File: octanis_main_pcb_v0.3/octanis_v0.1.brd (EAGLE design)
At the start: 95 x 48 mm, 89 parts, among them IC1 REG1117, IC2 LM555D, Q1 32.768kHz, T1 BC547, T2 BC547, U1 BQ24210, U2 BQ27510_DRZ_12, U3 DRV8836DSSR, U4 DRV8836DSSR, U5 DRV8836DSSR, U6 MSP430F5529IPNR, U7 DRV8836DSSR, U9 BMP180

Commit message: startet new mainboard PCB
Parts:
- removed BATTERY: - BAT +, pinhead:1X02
- removed C1, C2: 1uF, rcl:C1206
- removed C26: 12p, rcl:C0603
- removed C29: 100n, rcl:C0603
- removed C7, C8: 1uF, rcl:C0603
- removed CG1, CG3, CG6, CG7, CG8: 0.1uF, rcl:C0603
- removed CG2: 33nF, rcl:C0603
- removed CG4: 0.47uF, rcl:C0603
- removed DIGITAL1: DIGITAL1, pinhead:1X06
- removed HEATPAD: HEATPAD, con-molex:22-23-2021
- removed HUMIDITY: HS1101, rcl:C025-024X044
- removed I2C: SCL SDA, pinhead:1X02
- removed IC1: REG1117, burr-brown:SOT223
- removed IC2: LM555D, linear:SO08
- removed LED2: (no value), led:CHIP-LED0603
- removed Q1: 32.768kHz, crystal:FC-12M
- removed R28: 0R, rcl:R0603
- removed RG1: 1.8M, rcl:R0603
- removed RG2: 18.2k, rcl:R0603
- removed RG3, RH3: 1k, rcl:R0603
- removed RG5, RG6: 100, rcl:R0603
- removed RH1: 909k, rcl:R0603
- removed RH2: 576k, rcl:R0603
- removed RH4: 49.9k, rcl:R0603
- removed RSBAT: 0.01, resistor:R1206
- removed RT1: 21.5k, resistor:R1206
- removed RVDM: float, resistor:R1206
- removed SOLAR: - SOLAR +, pinhead:1X02
- removed T1, T2: BC547, transistor:TO92
- removed TEMP1, TEMP2: 103AT, varistor:RS-2,5
- removed U2: BQ27510_DRZ_12, bq27510_drz_12:DRZ12_1P95X2P45
- removed U6: MSP430F5529IPNR, TI_MSP430_v16_intern:PN80
- added C22, C9: 12p, rcl:C0402
- added C23: 100n, rcl:C0402
- added C24: 100n, rcl:C0603
- added D5: 1N581D1206, lpatiny:LED-1206
- added GREEN: 3V-ok, adafruit:CHIPLED_0603
- added JP3: (no value), pinhead:1X06
- added JP4: (no value), pinhead:2X07
- added LED0: LED0, adafruit:CHIPLED_0603
- added Q2: 32.768kHz, microcrystal:MS3V-T1R
- added R17, R8, R9: 1k, rcl:R0603
- added R18, RPUC1, RPUD1: 10k, rcl:R0603
- added R7: 0R, rcl:R0402
- added U$2: F54XX[A]---PZ100, TI_MSP430_v16:PZ100
- added U$3: SST25VF064C, BertaLib:SOIC_8-LEAD
- added U$4: HX1, Octanis1:HX1
- ANALOG: device pinhead:1X06 -> pinhead:1X08
- C25: value 12p -> 100n
- DIGITAL2: device pinhead:1X08 -> pinhead:1X11
- JP1: value rst SBW tst -> RST TST
- JP2: value SERIAL -> (none); device pinhead:1X04 -> pinhead:1X02
- LED1: value (none) -> LED1; device led:CHIP-LED0603 -> adafruit:CHIPLED_0603
- R1: value 1k -> 10k
- R16: value 1M -> 10k
- R2: value 1k -> 1M
- R4: value 500 -> 1k; device resistor:R1206 -> rcl:R0603
- U1: value BQ24210 -> SHT21; device bq24210_dqc_10:DQC10_P84X2P4 -> SENSIRION-SHT21:DFN300X300X110-7N
- moved LED1 178.5 mm to (1.27, -152.4), turned to 0 degrees
- moved R4 149.9 mm to (1.27, -134.6)
- moved R2 148.9 mm to (1.27, -123.2), flipped to the top
- moved U1 129.2 mm to (6.35, -108.0), turned to 0 degrees
- moved R1 124.1 mm to (14.0, -95.2), flipped to the top
- moved R16 115.3 mm to (14.0, -80.0), turned to 0 degrees
- moved JP2 109.1 mm to (1.98, -40.6), turned to 0 degrees
- moved C25 96.5 mm to (1.27, -73.7)
- moved DIGITAL2 28.4 mm to (57.1, 39.4)
- moved ANALOG 13.1 mm to (33.0, 39.4)
- moved JP1 10.3 mm to (43.2, 35.6)
- moved RPUD 5.68 mm to (61.0, 23.5)
- renumbered LED3 to RED
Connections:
- removed net 65: U6.65
- removed net 66: U6.66
- removed net 67: U6.67
- removed net AVCC: C29.1, R28.1, U6.11
- removed net BAT-: BATTERY.2, RG6.1, RSBAT.1
- removed net CHG_EN: U1.7, U6.5
- removed net EN_BAT_HEAT: T2.2
- removed net EN_SOLAR_HEAT: T1.2
- removed net HUMOUT: RH3.1
- removed net M1234SLEEP: U3.11, U3.12, U4.11, U4.12, U6.21
- removed net M5678SLEEP: U5.11, U5.12, U6.35, U7.11, U7.12
- removed net N$29: HUMIDITY.1, IC2.2, IC2.6, RH2.2
- removed net N$3: LED2.A, R2.1
- removed net N$33: RG2.1, RG3.2, TEMP2.1
- removed net N$34: CG1.1, RG3.1, U2.9
- removed net N$35: CG4.1, RG1.2, U2.2, U2.5
- removed net N$36: CG6.1, CG7.1, RG5.2, U2.8
- removed net N$37: HEATPAD.1, T1.1, T2.1
- removed net N$38: CG6.2, CG8.2, RG6.2, U2.7
- removed net N$8: RT1.2, U1.4
- removed net P2.7: DIGITAL1.6, U6.36
- removed net P3.0: DIGITAL1.5, U6.37
- removed net P3.1: DIGITAL1.4, U6.38
- removed net P3.2: DIGITAL1.3, U6.39
- removed net P3.3: DIGITAL1.2, U6.40
- removed net P3.4: DIGITAL1.1, U6.41
- removed net P3.5: U6.42
- removed net P3.6: U6.43
- removed net P3.7: U6.44
- removed net P5.0: ANALOG.2, U6.9
- removed net P5.1: ANALOG.1, U6.10
- removed net P5.4/XIN: C26.2, Q1.2, U6.12
- removed net P5.5/XOUT: C25.2, Q1.1, U6.13
- removed net P6.0: U6.77
- removed net P6.1: U6.78
- removed net P6.2: U6.79
- removed net P6.3: U6.80
- removed net P6.4: ANALOG.6, U6.1
- removed net P6.5: ANALOG.5, U6.2
- removed net P6.6: ANALOG.4, U6.3
- removed net P6.7: ANALOG.3, U6.4
- removed net RST/SBWTDIO: JP1.1, U6.76
- removed net SPI_CLK: JP2.1, U6.45
- removed net TARGET_DP: U6.62
- removed net TARGET_PUR: R16.2, U6.63
- removed net TEST/SBWTCK: JP1.2, U6.71
- removed net VCC: C1.1, SOLAR.2, T1.3, U1.1
- new net 3.3V: C3.1, GREEN.A, JP4.7, JP4.8, L1.P$1, R1.2, R16.2, R2.2, U$1.10, U$3.RST/HOLD, U$3.VDD, U$3.WP
- new net AVCC1: C23.1, R7.1, U$2.11
- new net CS: R17.2
- new net FMOSI: D5.A, R1.1, U$3.SI
- new net HX1EN: U$4.EN
- new net HX1TX: U$4.TXD
- new net LED0: LED0.A, U$2.9
- new net LED1: LED1.A, U$2.10
- new net M12SLEEP: U$2.18, U3.11, U3.12
- new net M34SLEEP: U$2.23, U4.11, U4.12
- new net M56SLEEP: U$2.40
- new net M78SLEEP: U$2.45, U5.11, U5.12, U7.11, U7.12
- new net N$28: ANALOG.7, U$2.98
- new net N$73: ANALOG.5, U$2.100
- new net N$74: ANALOG.4, U$2.1
- new net N$75: ANALOG.3, U$2.2
- new net N$76: ANALOG.2, U$2.3
- new net N$77: ANALOG.1, U$2.4
- new net N$78: DIGITAL2.10, U$2.77
- new net N$79: DIGITAL2.11, U$2.76
- new net P5.4/XIN1: C22.2, Q2.P2, U$2.13
- new net P5.5/XOUT1: C9.2, Q2.P1, U$2.14
- new net RFGND: U$4.RFGND
- new net RFGND2: U$4.RFGND2
- new net RST: JP1.1, U$2.96
- new net SCL2: JP4.2, RPUC.1, U$2.70
- new net SDA2: JP4.1, RPUD.1, U$2.69
- new net SPI_MISO: U$3.SO
- new net SPI_SCK: JP3.3, R18.1, U$2.68
- new net SPI_SIMO: D5.C, JP3.5, U$2.72
- new net SPI_SOMI: JP3.6, U$2.73
- new net TST: JP1.2, U$2.91
- net +3V3: now also C24.1, C25.1, R7.2, RPUC1.2, RPUD1.2, U$2.16, U$2.38, U$2.64, U$2.87; no longer C8.1, IC1.2, IC2.4, IC2.8, R28.2, RH4.1, U6.18, U6.50
- net +5V: now also JP4.13, JP4.14
- net 5VEN: now also R2.1; no longer U6.6
- net BAT+: now also U$4.VCC; no longer BATTERY.1, C2.1, C3.1, C7.1, CG3.1, IC1.3, L1.P$1, R1.2, R2.2, T2.3, U$1.10, U1.10, U2.3, U2.4
- net GND: now also C22.1, C23.2, C24.2, C25.2, C9.1, JP4.11, JP4.12, JP4.3, JP4.4, JP4.5, JP4.6, Q2.P3, R8.1, R9.1, U$2.12, U$2.15, U$2.37, U$2.63, U$2.88, U$3.VSS, U1.2; no longer C1.2, C2.2, C25.1, C26.1, C29.2, C7.2, C8.2, CG1.2, CG2.2, CG3.2, CG4.2, CG7.2, CG8.1, HEATPAD.2, HUMIDITY.2, IC1.1, IC2.1, R16.1, RG5.1, RH1.1, RSBAT.2, RVDM.1, SOLAR.1, TEMP1.1, TEMP2.2, U1.11, U1.3, U2.13, U2.6, U2.V, U2.V_2, U2.V_3, U2.V_4, U2.V_5, U2.V_6, U6.14, U6.19, U6.49, U6.61, U6.68
- net M1IN1: now also U$2.19; no longer U6.15
- net M1IN2: now also U$2.20; no longer U6.22
- net M2IN1: now also U$2.21; no longer U6.16
- net M2IN2: now also U$2.22; no longer U6.23
- net M3IN1: now also U$2.24; no longer U6.17
- net M3IN2: now also U$2.26; no longer U6.24
- net M4IN1: now also U$2.27; no longer U6.25
- net M4IN2: now also U$2.28; no longer U6.26
- net M5IN1: now also U$2.41; no longer U6.27
- net M5IN2: now also U$2.42; no longer U6.28
- net M6IN1: now also U$2.43; no longer U6.29
- net M6IN2: now also U$2.44; no longer U6.30
- net M7IN1: now also U$2.46; no longer U6.31
- net M7IN2: now also U$2.47; no longer U6.32
- net M8IN1: now also U$2.48; no longer U6.33
- net M8IN2: now also U$2.49; no longer U6.34
- net N$1: now also R18.2, U$3.SCK; no longer CG2.1, RG1.1, RG2.2, U2.1
- net N$10: now also R16.1, R17.1, U$3.CE; no longer R4.2, U1.2
- net N$14: now also U$2.86; no longer U6.60
- net N$15: now also U$2.85; no longer U6.59
- net N$2: now also U1.5; no longer LED1.A, R1.1
- net N$20: now also U$2.84; no longer U6.58
- net N$21: now also U$2.83; no longer U6.57
- net N$22: now also U$2.82; no longer U6.56
- net N$23: now also U$2.81; no longer U6.55
- net N$24: now also U$2.80; no longer U6.54
- net N$26: now also U$2.79; no longer U6.53
- net N$27: now also ANALOG.8, U$2.97; no longer IC2.5, RH1.2
- net N$30: now also ANALOG.6, U$2.99; no longer IC2.7, RH2.1, RH4.2
- net N$31: now also DIGITAL2.9, U$2.78; no longer IC2.3, RH3.2
- net N$4: now also GREEN.C, R4.2; no longer LED1.C, U1.8
- net N$5: now also LED0.C, R8.2; no longer LED2.C, U1.6
- net N$6: now also LED1.C, R9.2; no longer RVDM.2, U1.9
- net N$7: now also JP4.10, JP4.9; no longer RT1.1, TEMP1.2, U1.5
- net RX: now also JP2.1, U$2.54; no longer JP2.3, U6.52
- net SCL: now also JP3.1, RPUC1.1, U$2.35, U1.6; no longer I2C.1, RPUC.1, U2.11, U6.47
- net SDA: now also JP3.2, RPUD1.1, U$2.34, U1.1; no longer I2C.2, RPUD.1, U2.10, U6.46
- net SPI_SLAVE_EN: now also JP3.4, U$2.71; no longer JP2.4, U6.48
- net TX: now also U$2.53; no longer U6.51
- net VCORE: now also U$2.62; no longer U6.20
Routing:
- net BAT+: track 103.6 -> 0.00 mm, vias 3 -> 0
- net +5V: track 10.3 -> 59.3 mm, vias 0 -> 4
- net VCC: track 36.4 -> 0.00 mm
- net +3V3: track 7.05 -> 42.9 mm, vias 0 -> 2
- net M2IN2: track 0.00 -> 27.9 mm, vias 0 -> 2
- net M1IN2: track 0.00 -> 26.1 mm
- net M2IN1: track 0.00 -> 22.7 mm, vias 0 -> 2
- net CHG_EN: track 20.4 -> 0.00 mm, vias 4 -> 0
- net GND: track 39.7 -> 59.8 mm, vias 10 -> 19
- net N$1: track 17.0 -> 0.00 mm, vias 2 -> 0
- net N$7: track 16.7 -> 0.00 mm, vias 1 -> 0
- net N$38: track 16.6 -> 0.00 mm, vias 2 -> 0
- net N$49: track 0.00 -> 15.5 mm
- net N$58: track 0.00 -> 15.5 mm
- net M3IN2: track 0.00 -> 14.3 mm
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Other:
- board size 95 x 48 mm -> 94.9 x 47.8 mm

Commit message: added aria bob
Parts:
- removed RPUC1, RPUD1: 10k, rcl:R0603
- added RPUC2, RPUD2: 10k, rcl:R0603
- moved LED1 172.6 mm to (21.6, 19.1)
- moved R8 172.6 mm to (21.6, 25.4)
- moved LED0 172.6 mm to (21.6, 30.5)
- moved R4 172.6 mm to (21.6, 36.8)
- moved R9 172.6 mm to (21.6, 14.0)
- moved GREEN 158.9 mm to (8.89, 29.2)
- moved R2 149.2 mm to (15.2, 25.4)
- moved R1 145.9 mm to (90.2, 29.2)
- moved R16 145.9 mm to (90.2, 44.5)
- moved R17 145.9 mm to (77.5, 29.2)
- moved U1 145.9 mm to (82.5, 16.5)
- moved R18 145.9 mm to (83.8, 29.2)
- moved U$3 145.9 mm to (81.3, 36.8)
- moved D5 145.9 mm to (78.7, 24.1)
- moved JP2 101.5 mm to (88.3, 12.7)
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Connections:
- net +3V3: now also RPUC2.2, RPUD2.2; no longer RPUC1.2, RPUD1.2
- net SCL: now also RPUC.1; no longer RPUC1.1
- net SCL2: now also RPUC2.1; no longer RPUC.1
- net SDA: now also RPUD.1; no longer RPUD1.1
- net SDA2: now also RPUD2.1; no longer RPUD.1

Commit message: starting layout v0.3
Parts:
- removed R5: 68k, rcl:R0603
- removed RPUC2, RPUD2: 10k, rcl:R0603
- added C1: 100n, rcl:C0603
- added C2: 100nF, rcl:C0603
- added C26, C27, C28, C8: 470n, rcl:C0603
- added C7: 22uF, rcl:C0603
- added SJ1: (no value), jumper:SJ_2
- C15: value 0.1uF -> 100nF
- R3: value 270k -> 1M
- U$1: value TPS61230 -> TPS61232; device texas:DRC-S-PVSON-N11 -> texasinstruments:S-PVSON-N10
- moved C21 90.6 mm to (5.71, 35.6), turned to 0 degrees
- moved C17 85.5 mm to (11.4, 34.3), turned to 180 degrees
- moved MPU-6050 84.2 mm to (5.97, 30.6), turned to 90 degrees
- moved C16 82.2 mm to (11.4, 31.8), turned to 180 degrees
- moved C20 78.9 mm to (11.4, 29.2), turned to 0 degrees
- moved U9 75.5 mm to (3.58, 22.6), turned to 270 degrees
- moved C11 71.9 mm to (11.4, 23.6), turned to 0 degrees
- moved U1 71.3 mm to (15.2, 40.0)
- moved C10 69.6 mm to (8.26, 36.2)
- moved C13 69.6 mm to (8.26, 40.0)
- moved C15 69.6 mm to (7.62, 43.8)
- moved COMPASS 69.6 mm to (4.85, 40.3)
- moved R7 69.6 mm to (2.16, 44.7)
- moved C12 69.0 mm to (10.8, 21.0), turned to 180 degrees
- moved RPUD 54.3 mm to (1.91, 18.4), turned to 180 degrees
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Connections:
- net SPI_SLAVE_EN renamed SPI_EXTSLAVE_TE
- removed net BAT+: U$4.VCC
- removed net CS: R17.2
- removed net HX1TX: U$4.TXD
- removed net M12SLEEP: U$2.18, U3.11, U3.12
- removed net M34SLEEP: U$2.23, U4.11, U4.12
- removed net M56SLEEP: U$2.40
- removed net M78SLEEP: U$2.45, U5.11, U5.12, U7.11, U7.12
- removed net N$43: R3.1, R5.2, U$1.7
- removed net N$7: JP4.10, JP4.9
- removed net PG: U$1.5
- removed net RFGND2: U$4.RFGND2
- new net M1234SLEEP: U$2.24, U3.11, U3.12, U4.11, U4.12
- new net M5678SLEEP: U$2.50, U5.11, U5.12, U7.11, U7.12
- new net SPI_FLASH_CS: R17.2, U$2.75
- new net V_MOTOR: C26.2, C27.2, C28.2, C8.2, SJ1.2, U3.1, U4.1, U5.1, U7.1
- net +3V3: now also C1.1, C3.1, GREEN.A, JP4.10, JP4.7, JP4.8, JP4.9, L1.P$1, R1.2, R16.2, R2.2, SJ1.1, U$1.10, U$3.RST/HOLD, U$3.VDD, U1.5; no longer RPUC2.2, RPUD2.2
- net +5V: now also C2.1, C7.1, SJ1.3, U$1.7, U$4.VCC; no longer U3.1, U4.1, U5.1, U7.1
- net 3.3V: no longer C3.1, GREEN.A, JP4.7, JP4.8, L1.P$1, R1.2, R16.2, R2.2, U$1.10, U$3.RST/HOLD, U$3.VDD
- net 5VEN: now also U$2.17
- net GND: now also C1.2, C2.2, C26.1, C27.1, C28.1, C7.2, C8.1, U$1.EXPAD, U$4.0V; no longer R5.1, U$1.GND, U$1.GND@1, U$1.GND@2, U$1.GND@3, U$1.GND@4, U$1.GND@5
- net M1IN1: now also U$2.25; no longer U$2.19
- net M1IN2: now also U$2.26; no longer U$2.20
- net M2IN1: now also U$2.27; no longer U$2.21
- net M2IN2: now also U$2.28; no longer U$2.22
- net M3IN1: now also U$2.42; no longer U$2.24
- net M3IN2: now also U$2.43; no longer U$2.26
- net M4IN1: now also U$2.44; no longer U$2.27
- net M4IN2: now also U$2.45; no longer U$2.28
- net M5IN1: now also U$2.46; no longer U$2.41
- net M5IN2: now also U$2.47; no longer U$2.42
- net M6IN1: now also U$2.48; no longer U$2.43
- net M6IN2: now also U$2.49; no longer U$2.44
- net M7IN1: now also U$2.56; no longer U$2.46
- net M7IN2: now also U$2.57; no longer U$2.47
- net M8IN1: now also U$2.58; no longer U$2.48
- net M8IN2: now also U$2.59; no longer U$2.49
- net N$2: now also R3.1, U$1.5; no longer U1.5
- net RFGND: now also U$4.RFGND2
- net SCL: now also JP4.2
- net SCL2: no longer JP4.2, RPUC2.1
- net SDA: now also JP4.1
- net SDA2: no longer JP4.1, RPUD2.1
- net TX: now also U$4.TXD
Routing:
- net +5V: track 59.3 -> 117.7 mm, vias 4 -> 3
- net V_MOTOR: track 0.00 -> 41.6 mm, vias 0 -> 4
- net GND: track 59.8 -> 22.6 mm, vias 19 -> 13
- net 5VEN: track 0.00 -> 23.4 mm, vias 0 -> 2
- net M1234SLEEP: track 0.00 -> 22.0 mm, vias 0 -> 2
- net M5678SLEEP: track 0.00 -> 18.8 mm, vias 0 -> 2
- net N$43: track 16.9 -> 0.00 mm
- net M1IN1: track 0.00 -> 15.6 mm
- net M2IN2: track 27.9 -> 15.1 mm, vias 2 -> 0
- net SCL: track 12.4 -> 0.00 mm
- net M1IN2: track 26.1 -> 15.1 mm
- net SDA: track 10.7 -> 0.00 mm
- net M8IN1: track 10.4 -> 2.34 mm
- net M2IN1: track 22.7 -> 15.1 mm, vias 2 -> 0
- net +3V3: track 42.9 -> 35.8 mm, vias 2 -> 1
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- added copper zone on layer 1, net +3V3
- added copper zone on layer 1, net +5V
- added copper zone on layer 1, net GND
- added copper zone on layer 1, net IND
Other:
- board size 94.9 x 47.8 mm -> 94.9 x 48.4 mm

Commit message: layout done
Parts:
- removed D5: 1N581D1206, lpatiny:LED-1206
- removed R1, R18: 10k, rcl:R0603
- removed R17: 1k, rcl:R0603
- added SJ2: (no value), jumper:SJ
- C10: value 4.7uF -> 4.7u
- C11: value 0.1uF -> 100n
- C12: value 10uF -> 10u
- C13: value 0.22uF -> 220n
- C15, C16, C2, C20: value 100nF -> 100n
- C17: value 10nF -> 10n
- C21: value 2,2nF -> 2.2n
- C7: value 22uF -> 3 x 22uF
- DIGITAL2: value DIGITAL2 -> DIGITAL I/O
- JP2: value (none) -> TX RX
- JP3: value (none) -> SPI; device pinhead:1X06 -> pinhead:1X04
- U$2: value F54XX[A]---PZ100 -> MSP430F5438A
- moved C8 58.1 mm to (49.6, 5.18), turned to 270 degrees
- moved C26 52.4 mm to (39.5, 5.18), turned to 270 degrees
- moved C28 48.8 mm to (21.2, 6.30)
- moved C27 48.3 mm to (29.2, 5.18), turned to 270 degrees
- moved C1 38.5 mm to (12.1, 29.7), turned to 90 degrees
- moved R7 34.0 mm to (29.2, 24.1), turned to 180 degrees
- moved R16 30.8 mm to (63.4, 29.3)
- moved U$3 27.9 mm to (61.0, 23.5), turned to 180 degrees
- moved R4 25.6 mm to (25.5, 11.5), turned to 180 degrees
- moved GREEN 24.8 mm to (22.3, 11.6), turned to 270 degrees
- moved R3 24.1 mm to (16.6, 1.40), turned to 270 degrees
- moved JP3 23.7 mm to (55.8, 23.1), turned to 90 degrees
- moved C15 22.0 mm to (14.8, 23.0), turned to 0 degrees
- moved R9 21.4 mm to (33.8, 33.2), turned to 270 degrees
- moved C2 20.9 mm to (63.1, 3.33), turned to 90 degrees
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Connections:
- removed net FMOSI: D5.A, R1.1, U$3.SI
- removed net N$1: R18.2, U$3.SCK
- removed net N$10: R16.1, R17.1, U$3.CE
- removed net SPI_SIMO: D5.C, JP3.5, U$2.72
- removed net SPI_SOMI: JP3.6, U$2.73
- new net SPI_MOSI: JP3.3, U$2.72, U$3.SI
- net +3V3: no longer R1.2
- net 5VEN: now also U$2.23; no longer U$2.17
- net GND: now also SJ2.1
- net HX1EN: now also U$2.52
- net RFGND: now also SJ2.2
- net SCL: now also RPUD.1; no longer JP3.1, RPUC.1
- net SDA: now also RPUC.1; no longer JP3.2, RPUD.1
- net SPI_EXTSLAVE_TE: now also JP3.2; no longer JP3.4
- net SPI_FLASH_CS: now also R16.1, U$3.CE; no longer R17.2
- net SPI_MISO: now also JP3.4, U$2.73
- net SPI_SCK: now also JP3.1, U$3.SCK; no longer JP3.3, R18.1
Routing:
- net +3V3: track 35.8 -> 265.7 mm, vias 1 -> 5
- net RFGND: track 0.00 -> 105.4 mm
- net SDA: track 0.00 -> 94.7 mm, vias 0 -> 3
- net GND: track 22.6 -> 115.8 mm, vias 13 -> 35
- net SCL: track 0.00 -> 77.5 mm, vias 0 -> 5
- net N$79: track 0.00 -> 29.2 mm
- net N$78: track 0.00 -> 27.1 mm
- net N$31: track 0.00 -> 25.1 mm
- net HX1EN: track 0.00 -> 24.5 mm, vias 0 -> 2
- net N$77: track 0.00 -> 24.5 mm
- net TX: track 0.00 -> 24.2 mm
- net N$26: track 0.00 -> 23.0 mm
- net SPI_FLASH_CS: track 0.00 -> 21.4 mm
- net N$24: track 0.00 -> 21.0 mm
- net N$76: track 0.00 -> 20.8 mm
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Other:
- board size 94.9 x 48.4 mm -> 75.6 x 41.9 mm
- board text added: "5V 3.3V GND"
- board text added: "5V |GND| 3.3V | GND | I2C"
- board text added: "Octanis 1 v0.3"
- board text added: "SDA SCL"
- board text removed: "Octanis 1 v0.1"

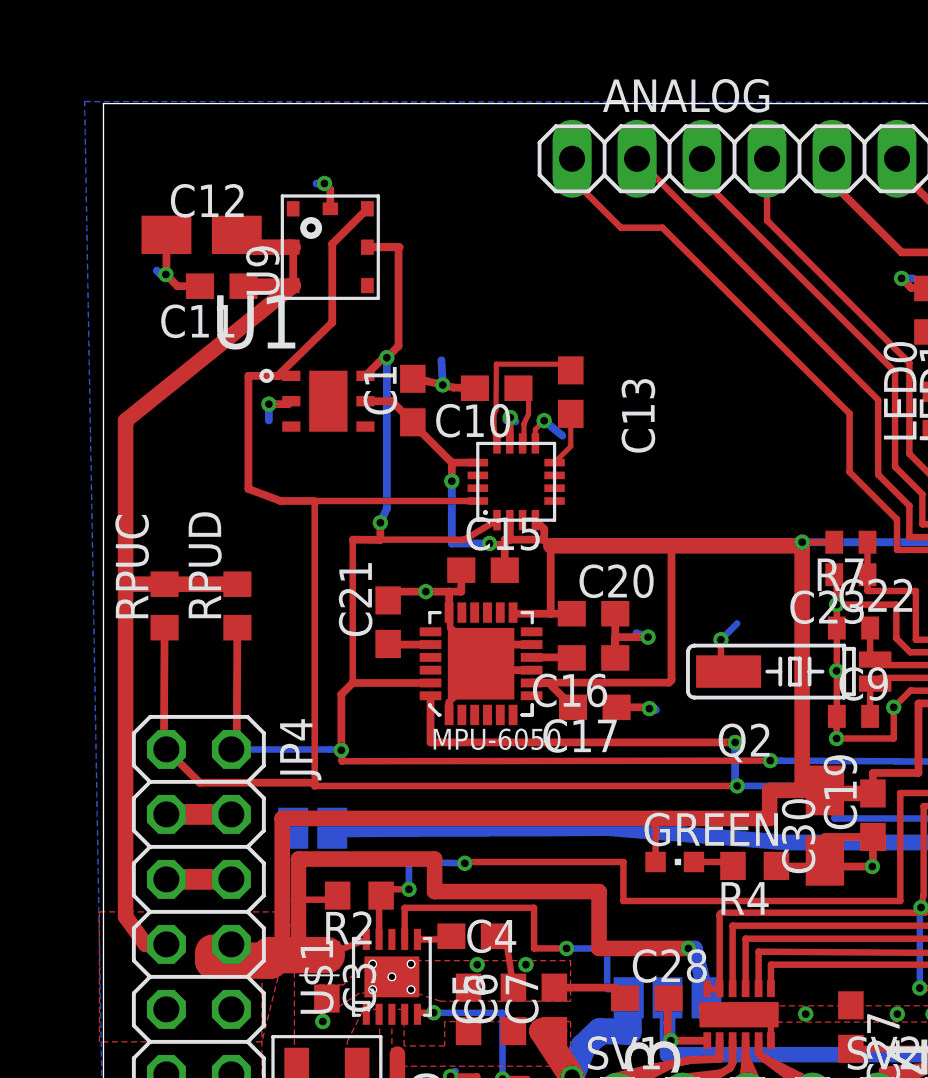
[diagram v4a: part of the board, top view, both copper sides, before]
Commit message: replaced sensirion humidity sensor with bosch
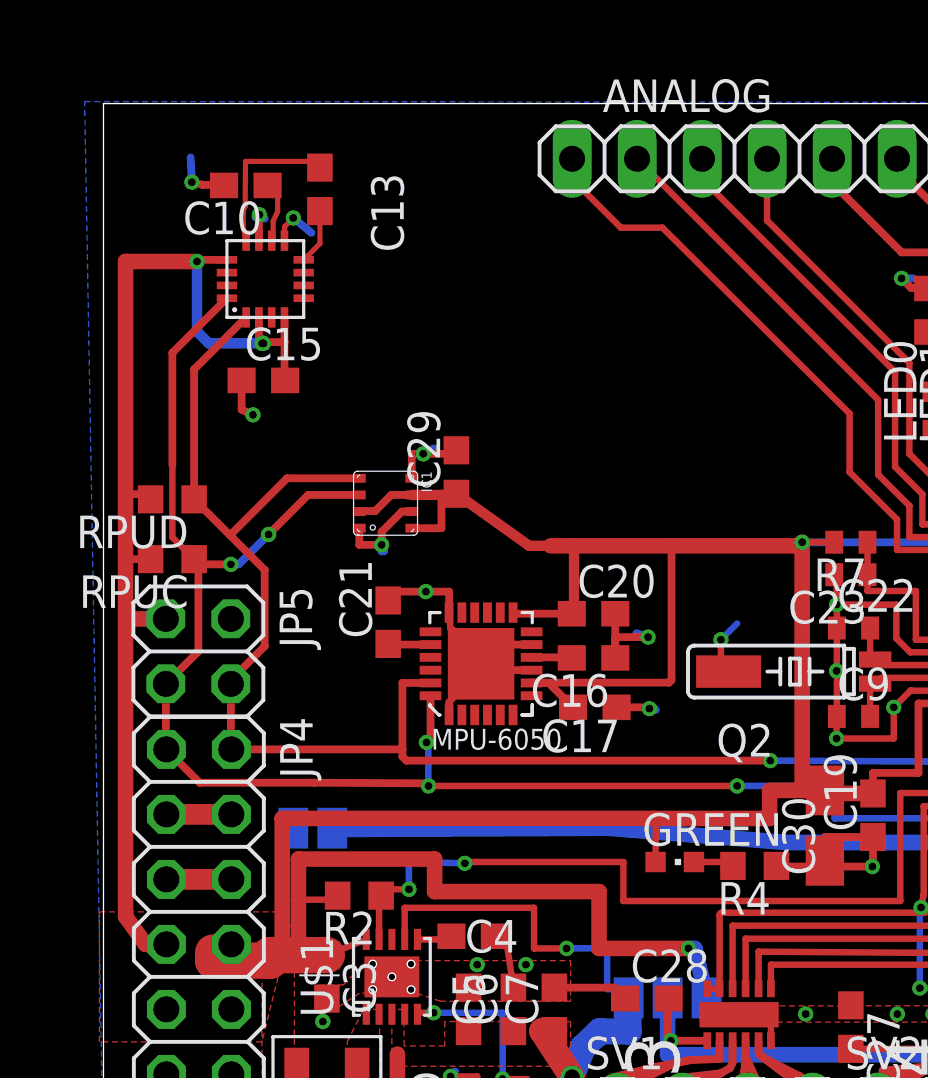
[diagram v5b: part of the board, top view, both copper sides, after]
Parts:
- removed C1, C11: 100n, rcl:C0603
- removed C12: 10u, resistor:A/3216-18R
- removed U1: SHT21, SENSIRION-SHT21:DFN300X300X110-7N
- removed U9: BMP180, SparkFun-Sensors:BMP180
- added C29: 100n, rcl:C0603
- added IC1: BME280, bosch-bme280:BME280
- added JP5: (no value), pinhead:2X02
- ANALOG: value ANALOG -> A7:A0
- moved C10 12.6 mm to (5.56, 38.1)
- moved COMPASS 12.6 mm to (6.32, 34.4)
- moved C13 12.6 mm to (8.46, 37.9)
- moved C15 11.3 mm to (6.25, 30.5)
- moved RPUD 4.88 mm to (2.69, 25.8), turned to 180 degrees
- moved RPUC 1.85 mm to (2.69, 23.5), turned to 180 degrees
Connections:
- net +3V3: now also C29.1, IC1.2, IC1.6, IC1.8, JP5.1; no longer C1.1, C11.1, C12.+, U1.5, U9.2, U9.3
- net GND: now also C29.2, IC1.1, IC1.5, IC1.7, JP5.2; no longer C1.2, C11.2, C12.-, U1.2, U9.7
- net SCL: now also IC1.4, JP5.4; no longer U1.6, U9.5
- net SDA: now also IC1.3, JP5.3; no longer U1.1, U9.6
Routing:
- net SDA: track 94.7 -> 71.4 mm, vias 3 -> 6
- net SCL: track 77.5 -> 68.3 mm, vias 5 -> 2
- net +3V3: track 265.7 -> 267.1 mm, vias 5 -> 6
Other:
- board text added: "5V |GND| 3.3V | GND | SDA | 3.3V"
- board text added: "SCL | GND"
- board text removed: "5V 3.3V GND"
- board text removed: "5V |GND| 3.3V | GND | I2C"
- board text removed: "SDA SCL"
